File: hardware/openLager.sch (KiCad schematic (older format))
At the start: 29 parts, among them J1 CONN_01X06, J2 DM3CS-SF, U1 STM32F411CEUx, U2 SPX3819M5-L-3-3, Y1 CSTCE8M00G15L99

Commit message: Adding BOM and tweaked solder paste layer
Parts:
- C1, C4: Link (none) -> https://octopart.com/cl05a106mp5nunc-samsung-22457395; Mfg Name (none) -> Samsung; Mfg PN (none) -> CL05A106MP5NUNC
- C3, C7, C8: Link (none) -> https://octopart.com/grm155r70j104ka01d-murata-17930200; Mfg Name (none) -> Murata; Mfg PN (none) -> GRM155R70J104KA01D
- C5: Link (none) -> https://octopart.com/grm155r70j105ma12d-murata-23261089; Mfg Name (none) -> Murata; Mfg PN (none) -> GRM155R70J105MA12D
- C6: Link (none) -> https://octopart.com/cl05a475mq5nqnc-samsung-24957780; Mfg Name (none) -> Samsung; Mfg PN (none) -> CL05A475MQ5NQNC
- D1: Link (none) -> https://octopart.com/aphhs1005cgck-kingbright-5355571; Mfg Name (none) -> Kingbright; Mfg PN (none) -> APHHS1005CGCK
- D2: Link (none) -> https://octopart.com/aphhs1005surck-kingbright-3990646; Mfg Name (none) -> Kingbright; Mfg PN (none) -> APHHS1005SURCK
- J1, TP1, TP2, TP3: Mfg Name (none) -> DNP; Mfg PN (none) -> DNP
- J2: Link (none) -> https://octopart.com/dm3cs-sf-hirose-44525751; Mfg Name (none) -> Hirose; Mfg PN (none) -> DM3CS-SF
- R1, R3, R4: Link (none) -> https://octopart.com/rc0402jr-0710kl-yageo-55458470; Mfg Name (none) -> Yageo; Mfg PN (none) -> RC0402JR-0710KL
- R10, R9: Link (none) -> https://octopart.com/rc0402jr-0747kl-yageo-39834460; Mfg Name (none) -> Yageo; Mfg PN (none) -> RC0402JR-0747KL
- R12, R13: Link (none) -> https://octopart.com/rc0402jr-07330rl-yageo-40021082; Mfg Name (none) -> Yageo; Mfg PN (none) -> RC0402JR-07330RL
- R2: Link (none) -> DNP; Mfg Name (none) -> DNP; Mfg PN (none) -> DNP
- R5, R6, R7, R8: Link (none) -> https://octopart.com/rc0402jr-0722rl-yageo-1173206; Mfg Name (none) -> Yageo; Mfg PN (none) -> RC0402JR-0722RL
- U1: Link (none) -> https://octopart.com/stm32f411ceu6-stmicroelectronics-47202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; Mfg Name (none) -> ST Microelectronics; Mfg PN (none) -> STM32F411CEU6
- U2: Link (none) -> https://octopart.com/spx3819m5-l-3-3%2Ftr-exar-9290124; Mfg Name (none) -> Exar; Mfg PN (none) -> SPX3819M5-L-3-3/TR
- Y1: Link (none) -> https://octopart.com/cstce8m00g15l99-r0-murata-17751576; Mfg Name (none) -> Murata; Mfg PN (none) -> CSTCE8M00G15L99-R0

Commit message: Clean up Link on J1 and TP*
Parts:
- J1, TP1, TP2, TP3: Link (none) -> DNP
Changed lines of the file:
@@
 F 4 "DNP" H 7250 7550 60  0001 C CNN "Mfg Name"
 F 5 "DNP" H 7250 7550 60  0001 C CNN "Mfg PN"
+F 6 "DNP" H 7250 7550 60  0001 C CNN "Link"
 	1    7250 7550
 	1    0    0    -1
@@
 F 4 "DNP" H 13750 7400 60  0001 C CNN "Mfg Name"
 F 5 "DNP" H 13750 7400 60  0001 C CNN "Mfg PN"
+F 6 "DNP" H 13750 7400 60  0001 C CNN "Link"
 	1    13750 7400
 	1    0    0    -1
@@
 F 4 "DNP" H 13950 7400 60  0001 C CNN "Mfg Name"
 F 5 "DNP" H 13950 7400 60  0001 C CNN "Mfg PN"
+F 6 "DNP" H 13950 7400 60  0001 C CNN "Link"
 	1    13950 7400
 	1    0    0    -1
@@
 F 4 "DNP" H 13900 4350 60  0001 C CNN "Mfg Name"
 F 5 "DNP" H 13900 4350 60  0001 C CNN "Mfg PN"
+F 6 "DNP" H 13900 4350 60  0001 C CNN "Link"
 	1    13900 4350
 	1    0    0    -1

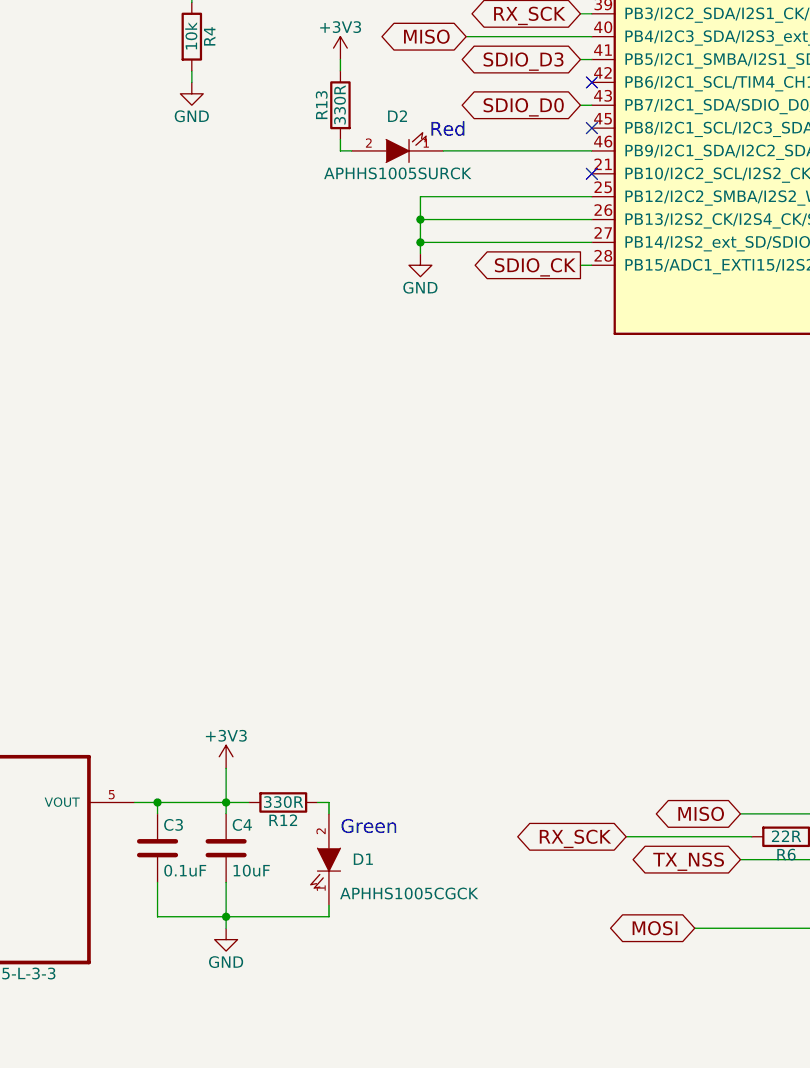
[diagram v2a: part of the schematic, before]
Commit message: Updated to RevB, changed LED and SS
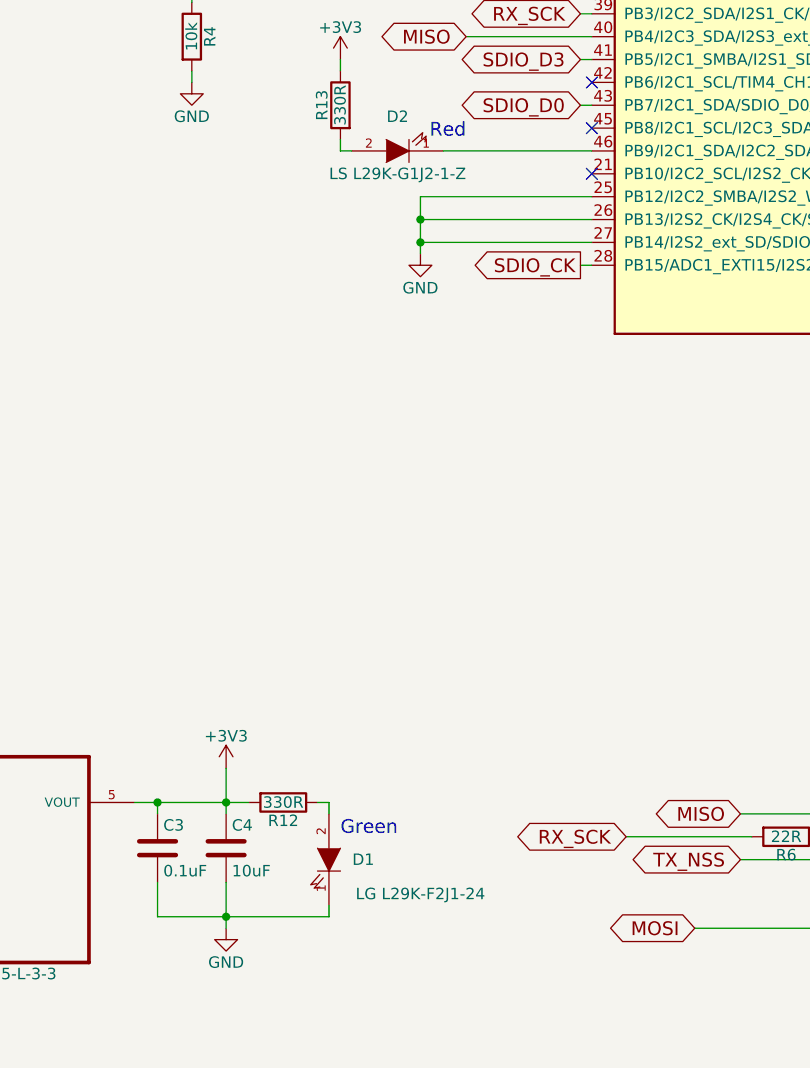
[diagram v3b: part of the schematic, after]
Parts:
- D1: value APHHS1005CGCK -> LG L29K-F2J1-24; Link https://octopart.com/aphhs1005cgck-kingbright-5355571 -> https://octopart.com/lg+l29k-f2j1-24-osram+opto-31119809; Mfg Name Kingbright -> Osram Opto; Mfg PN APHHS1005CGCK -> LG L29K-F2J1-24
- D2: value APHHS1005SURCK -> LS L29K-G1J2-1-Z; Link https://octopart.com/aphhs1005surck-kingbright-3990646 -> https://octopart.com/ls+l29k-g1j2-1-z-osram+opto-31093939; Mfg Name Kingbright -> Osram Opto; Mfg PN APHHS1005SURCK -> LS L29K-G1J2-1-Z
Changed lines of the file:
@@
 P 4050 7500
 F 0 "D1" V 4050 7650 50  0000 C CNN
-F 1 "APHHS1005CGCK" V 3900 7850 50  0000 C CNN
+F 1 "LG L29K-F2J1-24" V 3900 7900 50  0000 C CNN
 F 2 "openLagerFootprints:LED_0603" H 4050 7500 50  0001 C CNN
-F 3 "http://datasheet.octopart.com/APHHS1005CGCK-Kingbright-datasheet-17019150.pdf" H 4050 7500 50  0001 C CNN
-F 4 "Kingbright" H 4050 7500 60  0001 C CNN "Mfg Name"
-F 5 "APHHS1005CGCK" H 4050 7500 60  0001 C CNN "Mfg PN"
-F 6 "https://octopart.com/aphhs1005cgck-kingbright-5355571" H 4050 7500 60  0001 C CNN "Link"
+F 3 "http://datasheet.octopart.com/LG-L29K-F2J1-24-Osram-datasheet-41480516.pdf" H 4050 7500 50  0001 C CNN
+F 4 "Osram Opto" H 4050 7500 60  0001 C CNN "Mfg Name"
+F 5 "LG L29K-F2J1-24" H 4050 7500 60  0001 C CNN "Mfg PN"
+F 6 "https://octopart.com/lg+l29k-f2j1-24-osram+opto-31119809" H 4050 7500 60  0001 C CNN "Link"
 	1    4050 7500
 	0    1    -1   0
@@
 P 4350 4400
 F 0 "D2" H 4350 4250 50  0000 C CNN
-F 1 "APHHS1005SURCK" H 4350 4500 50  0000 C CNN
+F 1 "LS L29K-G1J2-1-Z" H 4350 4500 50  0000 C CNN
 F 2 "openLagerFootprints:LED_0603" H 4350 4400 50  0001 C CNN
-F 3 "http://datasheet.octopart.com/APHHS1005SURCK-Kingbright-datasheet-12529969.pdf" H 4350 4400 50  0001 C CNN
-F 4 "Kingbright" H 4350 4400 60  0001 C CNN "Mfg Name"
-F 5 "APHHS1005SURCK" H 4350 4400 60  0001 C CNN "Mfg PN"
-F 6 "https://octopart.com/aphhs1005surck-kingbright-3990646" H 4350 4400 60  0001 C CNN "Link"
+F 3 "http://datasheet.octopart.com/Q65110A1757-Osram-Opto-datasheet-31819788.pdf" H 4350 4400 50  0001 C CNN
+F 4 "Osram Opto" H 4350 4400 60  0001 C CNN "Mfg Name"
+F 5 "LS L29K-G1J2-1-Z" H 4350 4400 60  0001 C CNN "Mfg PN"
+F 6 "https://octopart.com/ls+l29k-g1j2-1-z-osram+opto-31093939" H 4350 4400 60  0001 C CNN "Link"
 	1    4350 4400
 	-1   0    0    1
